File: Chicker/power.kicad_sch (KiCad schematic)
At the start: 37 parts, among them U3 ZLDO1117QG33TA

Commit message: chicker v1.1 done (TM)
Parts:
- added H10, H11, H12: ToolingHoleJLC, bots:ToolingHoleJLC, symbol thebots_symlib:ToolingHoleJLC
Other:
- note added: "Tooling Holes for assembly orders"
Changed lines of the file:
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@@
+    (effects (font (size 1.27 1.27)) (justify left bottom))
+  )
+  (text "Tooling Holes\nfor assembly orders" (at 149.86 78.74 0)
     (effects (font (size 1.27 1.27)) (justify left bottom))
   )
@@
     )
   )
+  (symbol (lib_id "thebots_symlib:ToolingHoleJLC") (at 160.02 82.55 0) (unit 1)
+    (in_bom yes) (on_board yes) (dnp no) (fields_autoplaced)
+    (property "Reference" "H11" (at 162.56 81.28 0)
+      (effects (font (size 1.27 1.27)) (justify left) hide)
+    )
+    (property "Value" "ToolingHoleJLC" (at 160.02 78.105 0)
+      (effects (font (size 1.27 1.27)) hide)
+    )
+    (property "Footprint" "bots:ToolingHoleJLC" (at 160.02 82.55 0)
+      (effects (font (size 1.27 1.27)) hide)
+    )
+    (property "Datasheet" "~" (at 160.02 82.55 0)
+      (effects (font (size 1.27 1.27)) hide)
+    )
+    (instances
+      (project "chicker"
+        (path "/1a9ce3e8-a091-496c-9c5f-e7b2eb60e275/13b16574-f046-4bb6-b573-f06681d59f31"
+          (reference "H11") (unit 1)
+        )
+      )
+    )
+  )
   (symbol (lib_id "power:GND") (at 175.26 135.89 0) (unit 1)
     (in_bom yes) (on_board yes) (dnp no)
@@
         )
       )
+    )
+  )
+  (symbol (lib_id "thebots_symlib:ToolingHoleJLC") (at 166.37 82.55 0) (unit 1)
+    (in_bom yes) (on_board yes) (dnp no) (fields_autoplaced)
+    (property "Reference" "H12" (at 168.91 81.28 0)
+      (effects (font (size 1.27 1.27)) (justify left) hide)
+    )
+    (property "Value" "ToolingHoleJLC" (at 166.37 78.105 0)
+      (effects (font (size 1.27 1.27)) hide)
+    )
+    (property "Footprint" "bots:ToolingHoleJLC" (at 166.37 82.55 0)
+      (effects (font (size 1.27 1.27)) hide)
+    )
+    (property "Datasheet" "~" (at 166.37 82.55 0)
+      (effects (font (size 1.27 1.27)) hide)
+    )
+    (instances
+      (project "chicker"
+        (path "/1a9ce3e8-a091-496c-9c5f-e7b2eb60e275/13b16574-f046-4bb6-b573-f06681d59f31"
+          (reference "H12") (unit 1)
+        )
+      )
+    )
+  )
+  (symbol (lib_id "thebots_symlib:ToolingHoleJLC") (at 153.67 82.55 0) (unit 1)
+    (in_bom yes) (on_board yes) (dnp no) (fields_autoplaced)
+    (property "Reference" "H10" (at 156.21 81.28 0)
+      (effects (font (size 1.27 1.27)) (justify left) hide)
+    )
+    (property "Value" "ToolingHoleJLC" (at 153.67 78.105 0)
+      (effects (font (size 1.27 1.27)) hide)
+    )
+    (property "Footprint" "bots:ToolingHoleJLC" (at 153.67 82.55 0)
+      (effects (font (size 1.27 1.27)) hide)
+    )
+    (property "Datasheet" "~" (at 153.67 82.55 0)
+      (effects (font (size 1.27 1.27)) hide)
+    )
+    (instances
+      (project "chicker"
+        (path "/1a9ce3e8-a091-496c-9c5f-e7b2eb60e275/13b16574-f046-4bb6-b573-f06681d59f31"
+          (reference "H10") (unit 1)
+        )
+      )

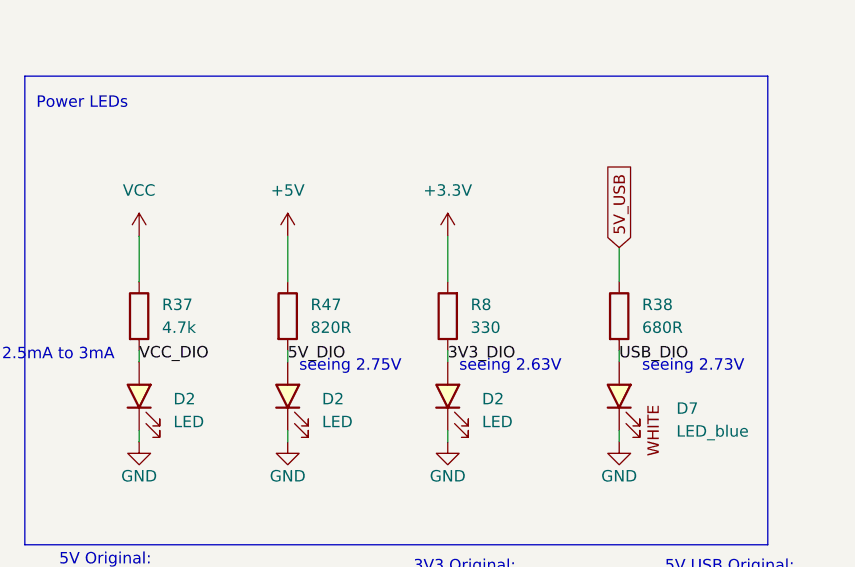
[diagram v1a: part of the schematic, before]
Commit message: code is functionally ready to test
after work tomorrow with an oscilloscope to figure out what is going on with the gate driver
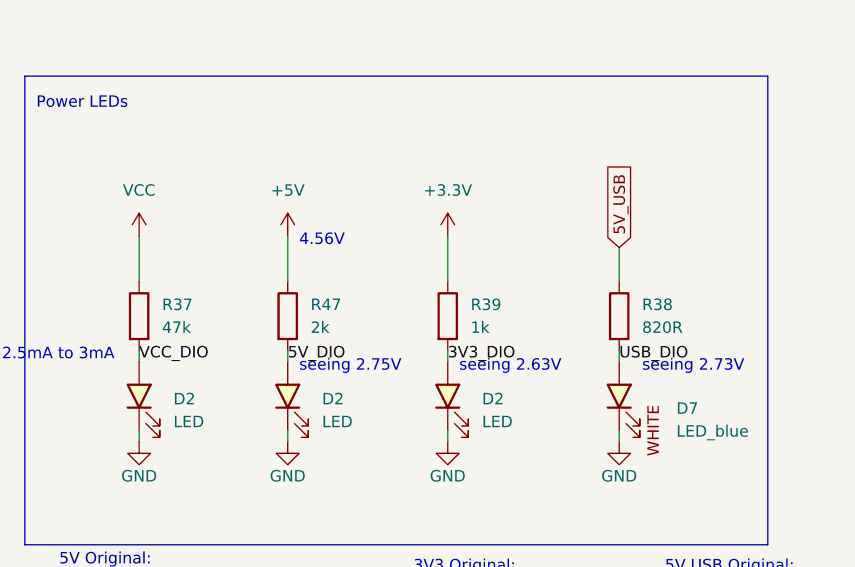
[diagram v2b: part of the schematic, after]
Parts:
- removed R37: 4.7k, bots:R_0603_1608Metric, symbol thebots_symlib:R_4.7k
- removed R38: 680R, bots:R_0603_1608Metric, symbol thebots_symlib:R_680R
- removed R47: 820R, bots:R_0603_1608Metric, symbol thebots_symlib:R_820R
- removed R8: 330, bots:R_0603_1608Metric, symbol bots:R_330R
- added R37: 47k, bots:R_0603_1608Metric, symbol thebots_symlib:R_47k
- added R38: 820R, bots:R_0603_1608Metric, symbol thebots_symlib:R_820R
- added R39: 1k, bots:R_0603_1608Metric, symbol thebots_symlib:R_1k
- added R47: 2k, bots:R_0603_1608Metric, symbol thebots_symlib:R_2k
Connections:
- net +3.3V: now also R39.1
- net +5V: now also R47.1
- net 3V3_DIO: now also R39.2
- net 5V_DIO: now also R47.2
- net 5V_USB: now also R38.1
- net USB_DIO: now also R38.2
- net VCC: now also R37.1
- net VCC_DIO: now also R37.2
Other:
- note added: "4.56V"

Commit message: chicker modifications (mostly ready to order)
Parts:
- removed U3: ZLDO1117QG33TA, bots:SOT-223-3_TabPin2, symbol thebots_symlib:ZLDO1117QG33TA
- added C42: 1u, bots:C_0603_1608Metric, symbol thebots_symlib:C_1u
- added C43: 0.01u, bots:C_0603_1608Metric, symbol thebots_symlib:C_0.01u
- added U11: MCP6231UT-E/OT, bots:SOT-23-5, symbol thebots_symlib:MCP6231UT-E/OT
- added U3: AMS1117, bots:SOT-223-3_TabPin2, symbol thebots_symlib:AMS1117-3.3
- R22: LCSC C22965 -> C25811
- renumbered C1 to C11, C1 to C12, D2 to D15, D2 to D6, D2 to D8, TP1 to TP2, TP1 to TP3, TP1 to TP4, TP1 to TP5
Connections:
- net +3.3V: now also C42.1, C43.1, U11.5, U3.2 (OUTPUT)
- net +5V: now also U3.3 (INPUT)
- net BATT_LEVEL: now also U11.3 (Vin-), U11.4 (Vout); no longer R22.1, R24.2
- net GND: now also C42.2, C43.2, U11.2, U3.1 (GND)
- net CHICKER_HV renamed KICK_HV
- net EXTRA_HV renamed CHIP_HV
- new net BATT_RAW: R22.1, R24.2, U11.1 (Vin+)
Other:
- moved on the sheet: R22, R23, R24, R51, R52

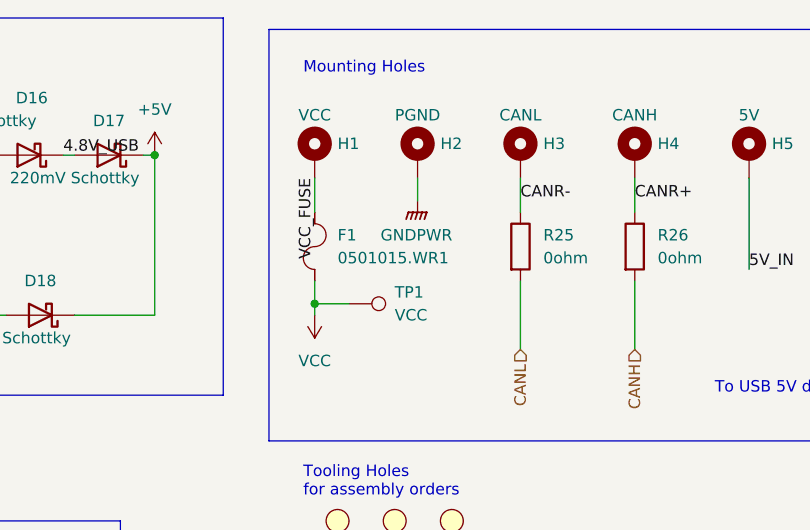
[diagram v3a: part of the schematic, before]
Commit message: fixed most issues with JLC ordering
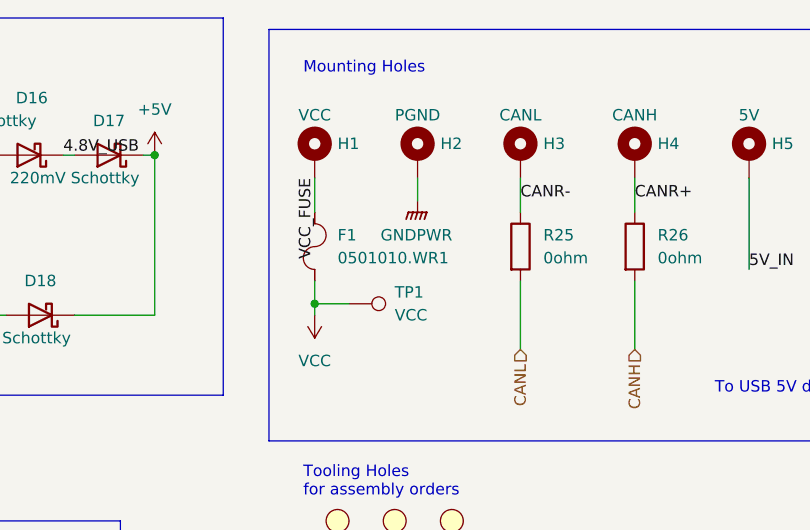
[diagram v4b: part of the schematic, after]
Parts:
- removed F1: 0501015.WR1, bots:Fuse_1206_3216Metric, symbol bots:Fuse_0501015.WR1
- added F1: 0501010.WR1, bots:Fuse_1206_3216Metric, symbol thebots_symlib:Fuse_0501010.WR1
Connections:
- net VCC: now also F1.1
- net VCC_FUSE: now also F1.2

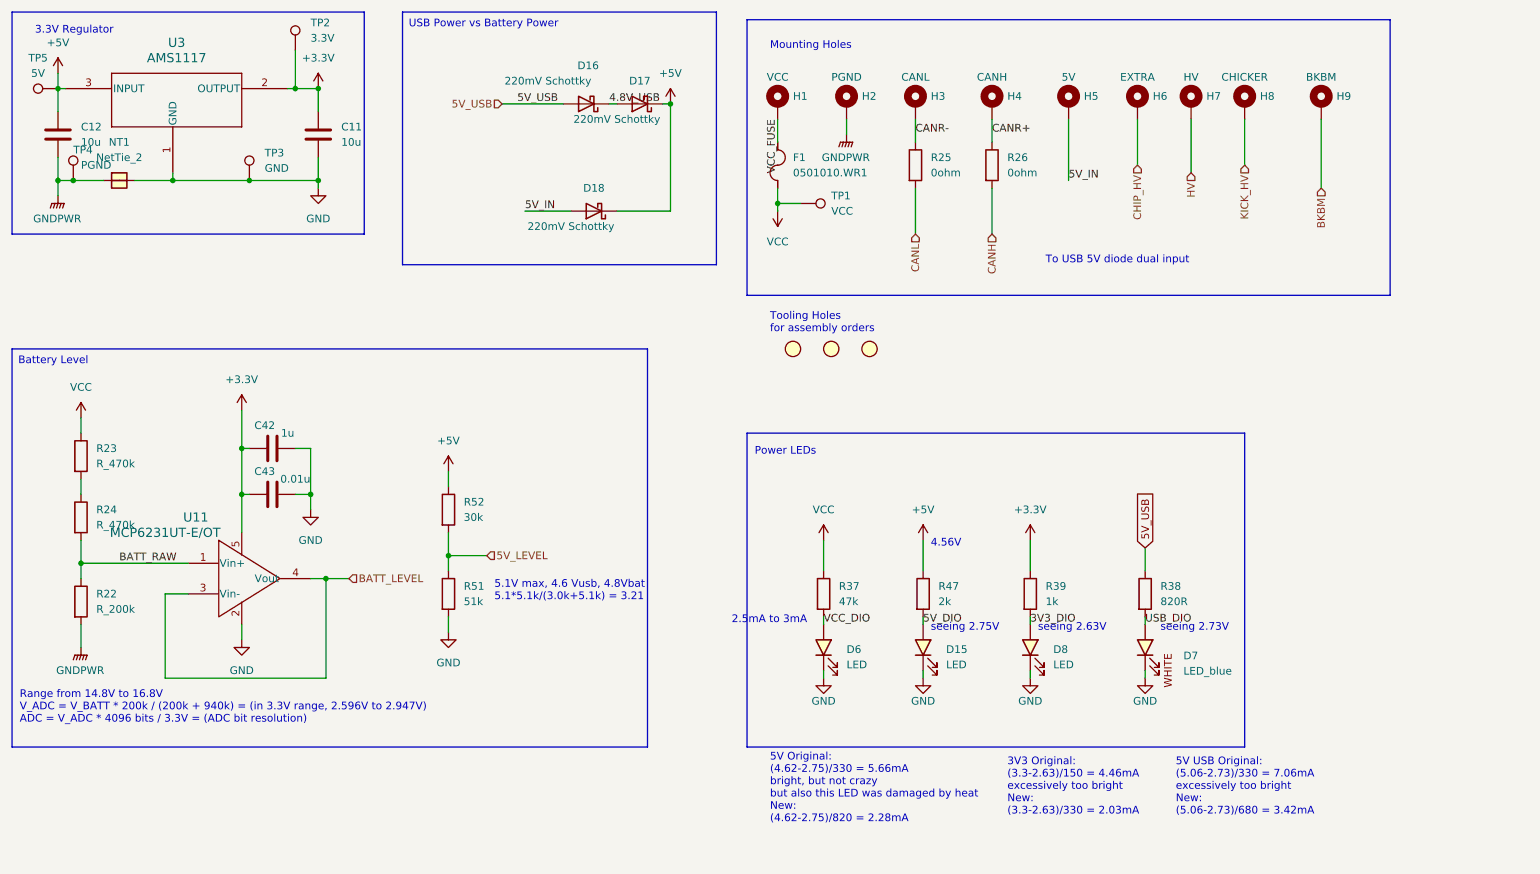
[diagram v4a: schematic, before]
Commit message: ESD+schematic fixes
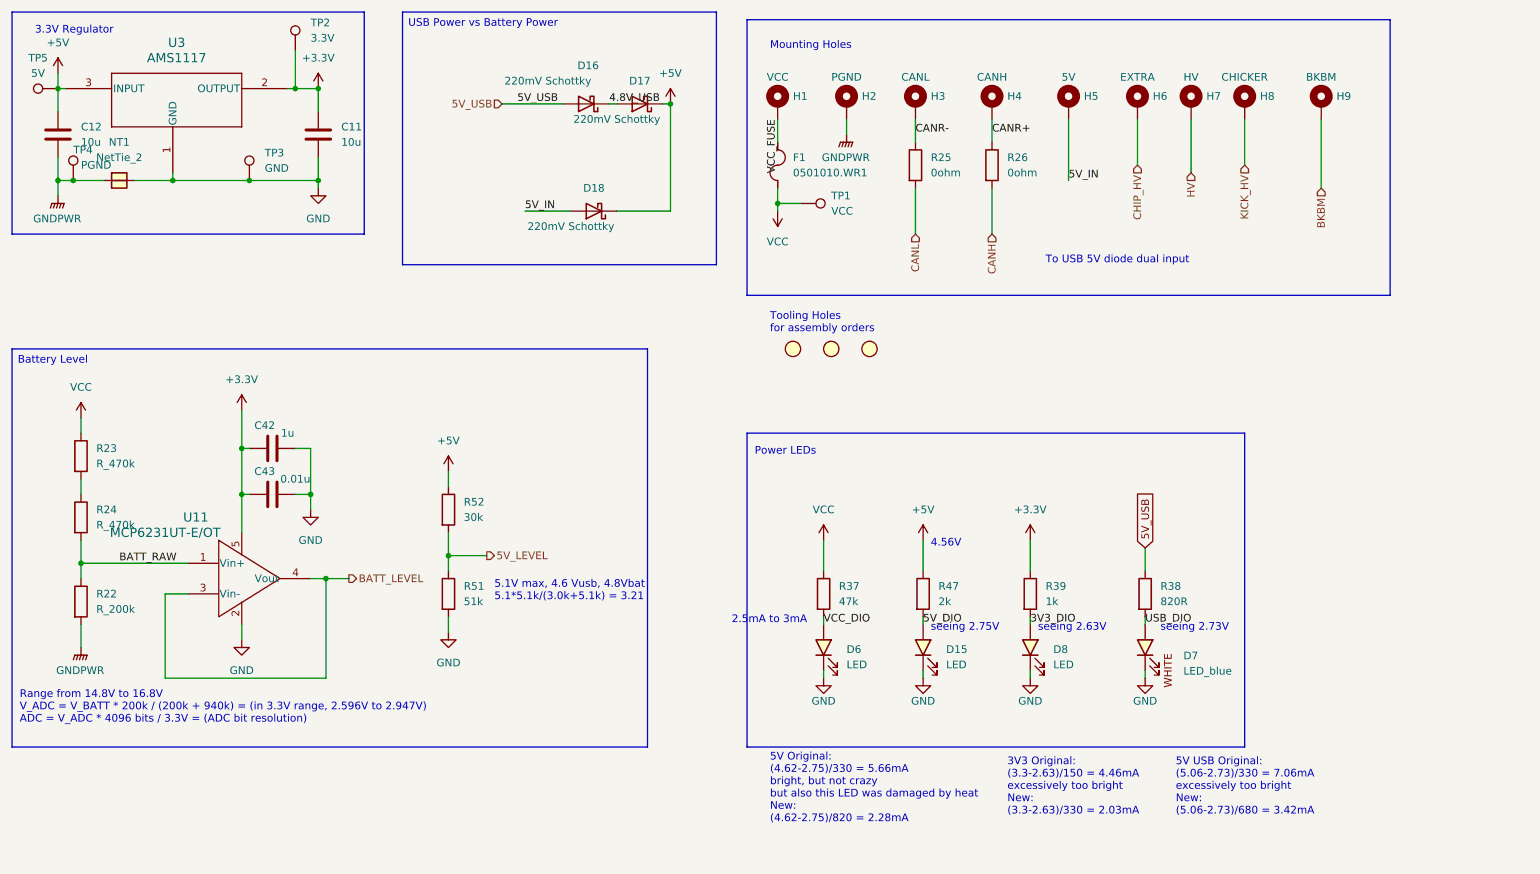
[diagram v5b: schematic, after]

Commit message: chicker v1.1 basic parts
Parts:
- removed U3: AMS1117, bots:SOT-223-3_TabPin2, symbol thebots_symlib:AMS1117-3.3
- added U3: AMS1117-3.3, bots:SOT-223-3_TabPin2, symbol bots:AMS1117-3.3
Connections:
- net +3.3V: now also U3.2 (OUTPUT)
- net +5V: now also U3.3 (INPUT)
- net GND: now also U3.1 (GND)
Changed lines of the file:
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@@
+	)
+	(symbol
+		(lib_id "bots:AMS1117-3.3")
+		(at 50.8 38.1 0)
+		(unit 1)
+		(exclude_from_sim no)
+		(in_bom yes)
+		(on_board yes)
+		(dnp no)
+		(fields_autoplaced yes)
+		(property "Reference" "U3"
+			(at 51.435 30.48 0)
+			(effects
+				(font
+					(size 1.524 1.524)
+				)
+			)
+		)
+		(property "Value" "AMS1117-3.3"
+			(at 51.435 33.02 0)
+			(effects
+				(font
+					(size 1.524 1.524)
+				)
+			)
+		)
+		(property "Footprint" "bots:SOT-223-3_TabPin2"
+			(at 17.78 40.64 0)
+			(effects
+				(font
+					(size 1.27 1.27)
+					(italic yes)
+				)
+				(hide yes)
+			)
+		)
+		(property "Datasheet" ""
+			(at 17.78 40.64 0)
+			(effects
+				(font
+					(size 1.27 1.27)
+					(italic yes)
+				)
+				(hide yes)
+			)
+		)
+		(property "Description" ""
+			(at 50.8 38.1 0)
+			(effects
+				(font
+					(size 1.27 1.27)
+				)
+				(hide yes)
+			)
+		)
+		(property "MPN" " AMS1117-3.3"
+			(at 50.8 38.1 0)
+			(effects
+				(font
+					(size 1.27 1.27)
+				)
+				(hide yes)
+			)
+		)
+		(property "Manufacturer" "Advanced Monolithic Systems"
+			(at 50.8 38.1 0)
+			(effects
+				(font
+					(size 1.27 1.27)
+				)
+				(hide yes)
+			)
+		)
+		(property "Price" "0.179"
+			(at 50.8 38.1 0)
+			(effects
+				(font
+					(size 1.27 1.27)
+				)
+				(hide yes)
+			)
+		)
+		(property "JLC" " SOT-223"
+			(at 50.8 38.1 0)
+			(effects
+				(font
+					(size 1.27 1.27)
+				)
+				(hide yes)
+			)
+		)
+		(property "LCSC" "C6186"
+			(at 50.8 38.1 0)
+			(effects
+				(font
+					(size 1.27 1.27)
+				)
+				(hide yes)
+			)
+		)
+		(property "JLC Extended" "no"
+			(at 50.8 38.1 0)
+			(effects
+				(font
+					(size 1.27 1.27)
+				)
+				(hide yes)
+			)
+		)
+		(pin "3"
+		)
+		(pin "2"
+		)
+		(pin "1"
+		)
+		(instances
+			(project ""
+				(path "/1a9ce3e8-a091-496c-9c5f-e7b2eb60e275/13b16574-f046-4bb6-b573-f06681d59f31"
+					(reference "U3")
+					(unit 1)
+				)
+			)
+		)
 	)
 	(symbol
@@
 					(unit 1)
 				)
-			)
-		)
-	)
-	(symbol
-		(lib_id "thebots_symlib:AMS1117-3.3")
-		(at 50.8 38.1 0)
-		(unit 1)
-		(exclude_from_sim no)
-		(in_bom yes)
-		(on_board yes)
-		(dnp no)
-		(fields_autoplaced yes)
-		(property "Reference" "U3"
-			(at 51.435 30.48 0)
-			(effects
-				(font
-					(size 1.524 1.524)
-				)
-			)
-		)
-		(property "Value" "AMS1117"
-			(at 51.435 33.02 0)
-			(effects
-				(font
-					(size 1.524 1.524)
-				)
-			)
-		)
-		(property "Footprint" "bots:SOT-223-3_TabPin2"
-			(at 17.78 40.64 0)
-			(effects
-				(font
-					(size 1.27 1.27)
-					(italic yes)
-				)
-				(hide yes)
-			)
-		)
-		(property "Datasheet" ""
-			(at 17.78 40.64 0)
-			(effects
-				(font
-					(size 1.27 1.27)
-					(italic yes)
-				)
-				(hide yes)
-			)
-		)
-		(property "Description" ""
-			(at 50.8 38.1 0)
-			(effects
-				(font
-					(size 1.27 1.27)
-				)
-				(hide yes)
-			)
-		)
-		(property "MPN" "AMS1117-3.3 "
-			(at 50.8 38.1 0)
-			(effects
-				(font
-					(size 1.27 1.27)
-				)
-				(hide yes)
-			)
-		)
-		(property "Manufacturer" "onsemi"
-			(at 50.8 38.1 0)
-			(effects
-				(font
-					(size 1.27 1.27)
-				)
-				(hide yes)
-			)
-		)
-		(property "Price" "0.32"
-			(at 50.8 38.1 0)
-			(effects
-				(font
-					(size 1.27 1.27)
-				)
-				(hide yes)
-			)
-		)
-		(property "JLC" "SOT-223"
-			(at 50.8 38.1 0)
-			(effects
-				(font
-					(size 1.27 1.27)
-				)
-				(hide yes)
-			)
-		)
-		(property "LCSC" "C6186"
-			(at 50.8 38.1 0)
-			(effects
-				(font
-					(size 1.27 1.27)
-				)
-				(hide yes)
-			)
-		)
-		(property "JLC Extended" "yes"
-			(at 50.8 38.1 0)
-			(effects
-				(font
-					(size 1.27 1.27)
-				)
-				(hide yes)
-			)
-		)
-		(pin "1"
-		)
-		(pin "2"
-		)
-		(pin "3"
-		)
-		(instances
-			(project "chicker"
-				(path "/1a9ce3e8-a091-496c-9c5f-e7b2eb60e275/13b16574-f046-4bb6-b573-f06681d59f31"
-					(reference "U3")
-					(unit 1)
-				)
